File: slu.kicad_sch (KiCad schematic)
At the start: 166 parts, among them sw1 sw_2pos

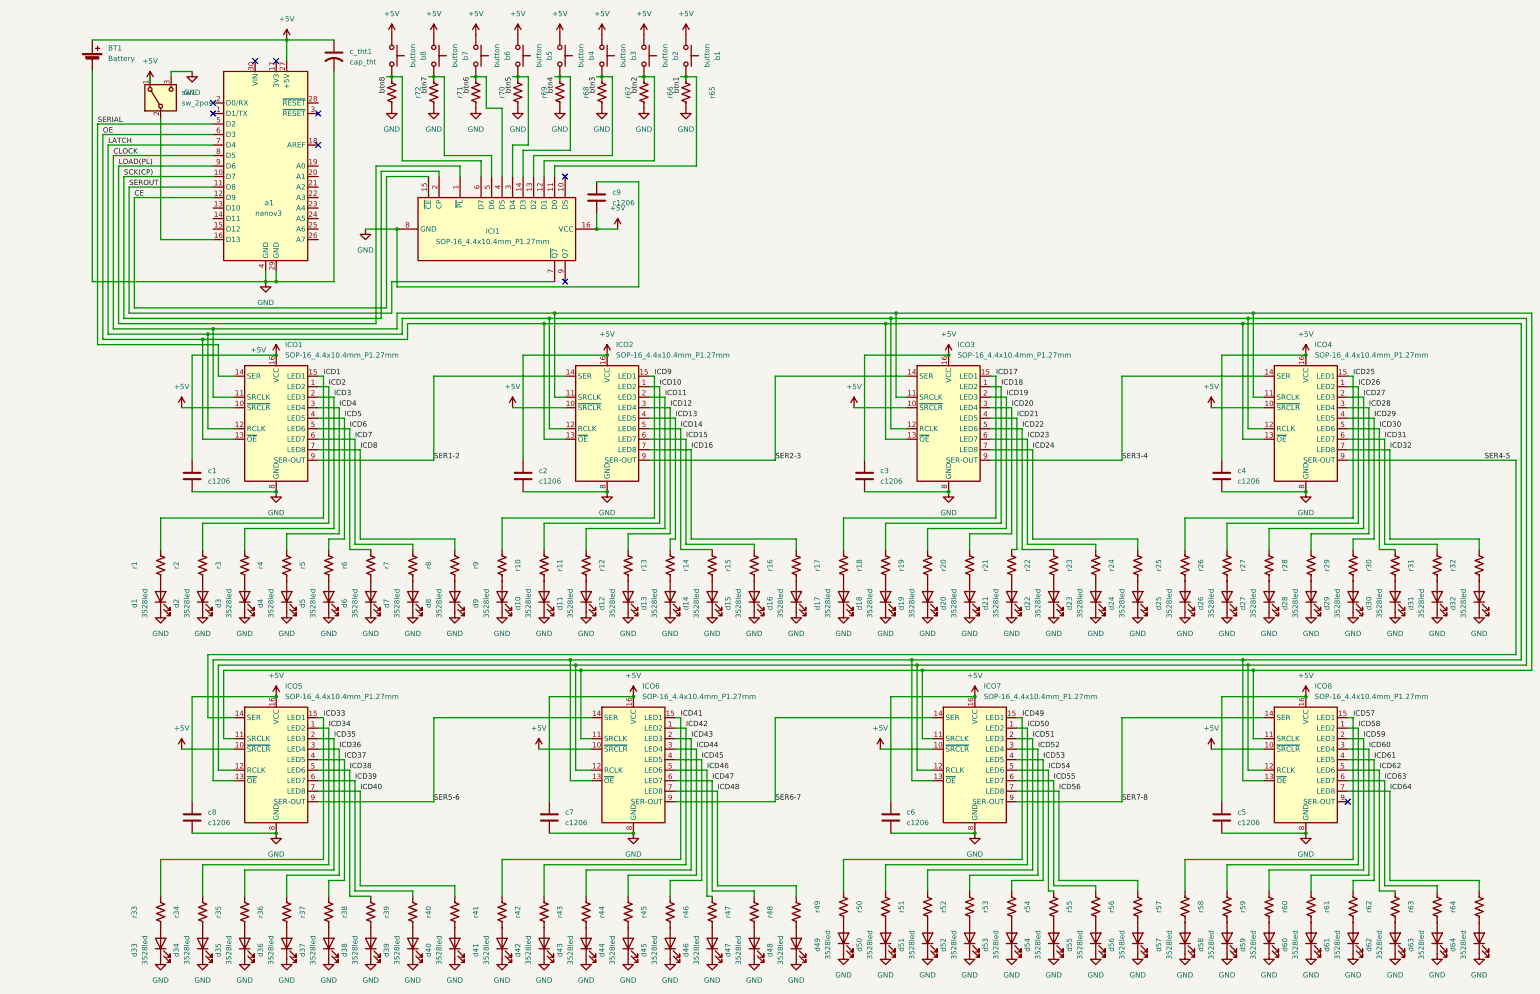
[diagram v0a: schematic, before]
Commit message: first finished draft all tracks connected
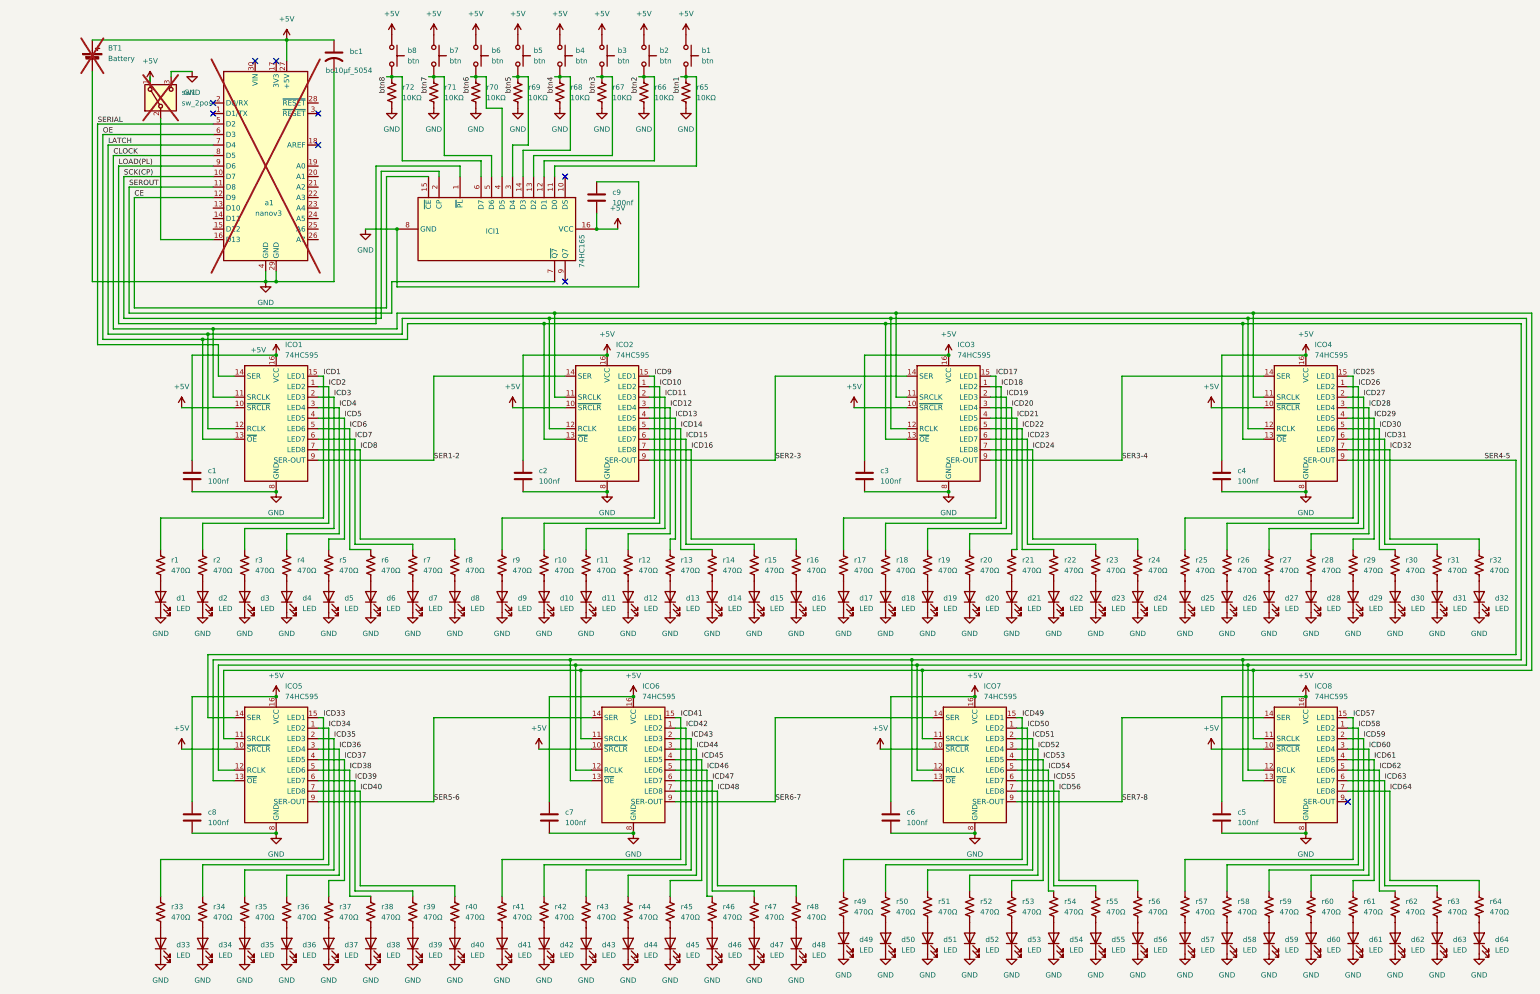
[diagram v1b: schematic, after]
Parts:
- BT1, a1, sw1: now not fitted; now left out of the parts list
- ICI1: value SOP-16_4.4x10.4mm_P1.27mm -> 74HC165; footprint Package_SO:SO-16_3.9x9.9mm_P1.27mm -> slu_leds_lib:sop16_hc165; symbol a_detolib_sym:74HC165 -> slu_leds_sym:ici_hc165; JLCPCB Part# (none) -> C22384789
- ICO1, ICO2, ICO3, ICO4, ICO5, ICO6, ICO7, ICO8: value SOP-16_4.4x10.4mm_P1.27mm -> 74HC595; footprint Package_SO:SOP-16_4.4x10.4mm_P1.27mm -> slu_leds_lib:sop16_hc595; symbol a_detolib_sym:74HC595D -> slu_leds_sym:ico_hc595; JLCPCB Part# (none) -> C10092
- b1, b2, b3, b4, b5, b6, b7, b8: value button -> btn; footprint a_detolib:btn_4x3 -> slu_leds_lib:btn_4x3; symbol a_detolib_sym:button -> slu_leds_sym:btn; JLCPCB Part# (none) -> C720477
- bc1: renamed from c_tht1; value cap_tht -> bc10µf_5054; footprint a_detolib:CP_Elec_5x5.4 -> slu_leds_lib:bulkcap_smd; symbol a_detolib_sym:bulk_cap_smd -> slu_leds_sym:bc10µf_5054; JLCPCB Part# (none) -> C72487
- c1, c2, c3, c4, c5, c6, c7, c8, c9: value c1206 -> 100nf; symbol a_detolib_sym:c1206 -> slu_leds_sym:c100nf_1206; JLCPCB Part# (none) -> C24497
- d1, d10, d11, d12, d13, d14, d15, d16, d17, d18, d19, d2, d20, d21, d22, d23, d24, d25, d26, d27, d28, d29, d3, d30, d31, d32, d33, d34, d35, d36, d37, d38, d39, d4, d40, d41, d42, d43, d44, d45, d46, d47, d48, d49, d5, d50, d51, d52, d53, d54, d55, d56, d57, d58, d59, d6, d60, d61, d62, d63, d64, d7, d8, d9: value 3528led -> LED; footprint a_detolib:3528led -> slu_leds_lib:blue_led_3528; symbol a_detolib_sym:led_3528 -> slu_leds_sym:led_3528; JLCPCB Part# (none) -> C2843802
- r1, r10, r11, r12, r13, r14, r15, r16, r17, r18, r19, r2, r20, r21, r22, r23, r24, r25, r26, r27, r28, r29, r3, r30, r31, r32, r33, r34, r35, r36, r37, r38, r39, r4, r40, r41, r42, r43, r44, r45, r46, r47, r48, r49, r5, r50, r51, r52, r53, r54, r55, r56, r57, r58, r59, r6, r60, r61, r62, r63, r64, r7, r8, r9: value ~ -> 470Ω; footprint a_detolib:r1206 -> slu_leds_lib:r_470Ω_1206; symbol a_detolib_sym:r1206 -> slu_leds_sym:r470_1206; JLCPCB Part# (none) -> C4502
- r65, r66, r67, r68, r69, r70, r71, r72: value ~ -> 10KΩ; footprint a_detolib:r1206 -> slu_leds_lib:r_10KΩ_1206; symbol a_detolib_sym:r1206 -> slu_leds_sym:r10k_1206; JLCPCB Part# (none) -> C17902

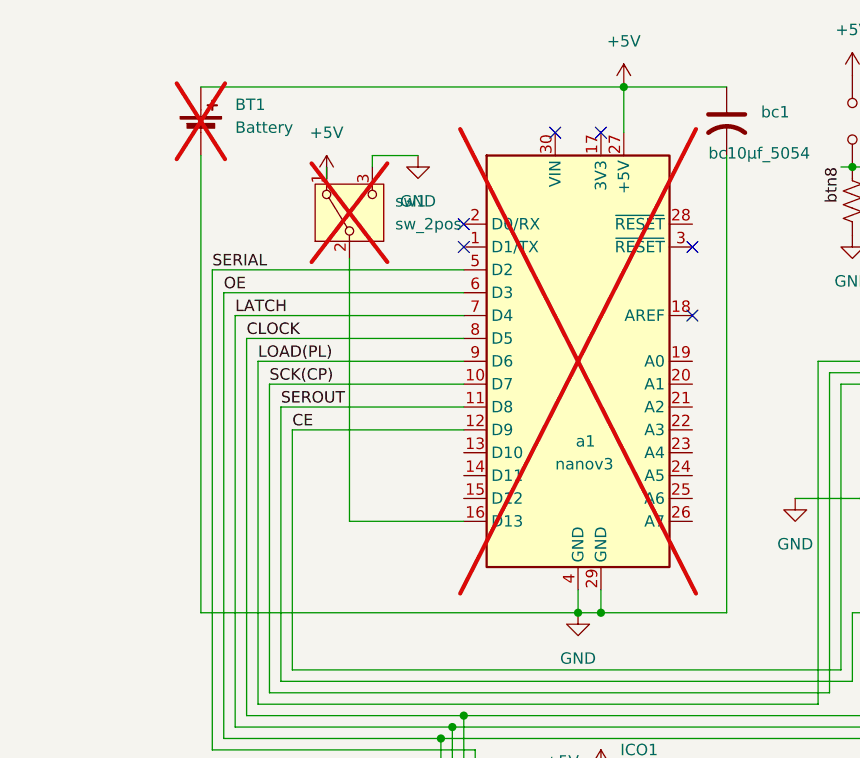
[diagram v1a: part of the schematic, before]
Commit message: most drc flags fixed
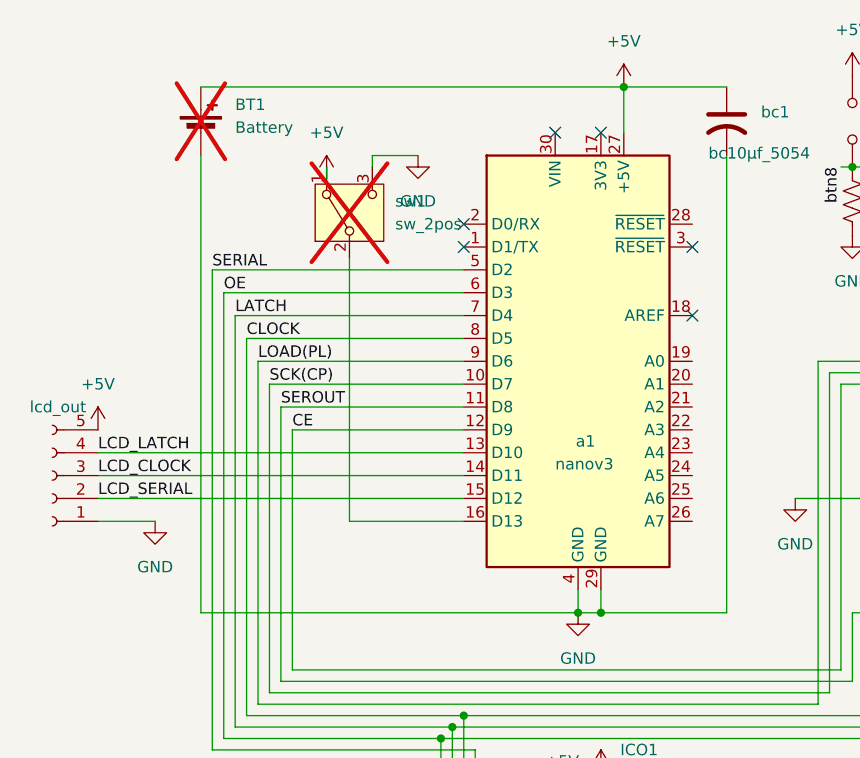
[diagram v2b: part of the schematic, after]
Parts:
- added J1: lcd_out, a_detolib:5pin_2.54, symbol slu_leds_sym:lcd_out
- a1: now fitted
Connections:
- net +5V: now also J1.5 (Pin_5)
- net GND: now also J1.1 (Pin_1)
- net LCD_LATCH: now reaches a1.13 (D10)
- net LCD_LATCH: now also J1.4 (Pin_4)
- net LCD_CLOCK: now reaches a1.14 (D11)
- net LCD_CLOCK: now also J1.3 (Pin_3)
- net LCD_SERIAL: now reaches a1.15 (D12)
- net LCD_SERIAL: now also J1.2 (Pin_2)

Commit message: almost done
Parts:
- added DIO1: SS34, slu_leds_lib:D_SMA, symbol slu_leds_sym:SS34
- BT1: footprint a_detolib:btry_18650_foirot -> slu_leds_lib:btry_18650_foirot; now fitted
- sw1: now fitted
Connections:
- net +5V: now also DIO1.1 (K); no longer BT1.1 (+)
- new net battery power: BT1.1 (+), DIO1.2 (A)
- no-connect marks 9 -> 18
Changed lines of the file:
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@@
 	)
 	(no_connect
+		(at 86.36 60.96)
+	)
+	(no_connect
 		(at 60.96 40.64)
 	)
@@
 	)
 	(no_connect
+		(at 86.36 68.58)
+	)
+	(no_connect
+		(at 86.36 63.5)
+	)
+	(no_connect
 		(at 60.96 38.1)
 	)
@@
 	)
 	(no_connect
+		(at 86.36 71.12)
+	)
+	(no_connect
+		(at 86.36 53.34)
+	)
+	(no_connect
+		(at 86.36 66.04)
+	)
+	(no_connect
+		(at 86.36 55.88)
+	)
+	(no_connect
+		(at 86.36 38.1)
+	)
+	(no_connect
 		(at 86.36 48.26)
 	)
@@
 		(at 146.05 55.88)
 	)
+	(no_connect
+		(at 86.36 58.42)
+	)
 	(wire
 		(pts
@@
 	(wire
 		(pts
-			(xy 31.75 22.86) (xy 78.74 22.86)
+			(xy 90.17 223.52) (xy 68.58 223.52)
 		)
 		(stroke
@@
 	(wire
 		(pts
-			(xy 90.17 223.52) (xy 68.58 223.52)
+			(xy 53.34 22.86) (xy 78.74 22.86)
 		)
 		(stroke
@@
 	(wire
 		(pts
-			(xy 31.75 30.48) (xy 31.75 81.28)
+			(xy 31.75 34.29) (xy 31.75 81.28)
 		)
 		(stroke
@@
 	(wire
 		(pts
+			(xy 31.75 22.86) (xy 45.72 22.86)
+		)
+		(stroke
+			(width 0)
+			(type default)
+		)
+	)
+	(wire
+		(pts
 			(xy 226.06 88.9) (xy 226.06 109.22)
 		)
@@
 	(wire
 		(pts
+			(xy 31.75 26.67) (xy 31.75 22.86)
+		)
+		(stroke
+			(width 0)
+			(type default)
+		)
+	)
+	(wire
+		(pts
 			(xy 176.53 223.52) (xy 151.13 223.52)
 		)
@@
 		)
 	)
+	(label "battery power"
+		(at 31.75 22.86 0)
+		(effects
+			(font
+				(size 1.27 1.27)
+			)
+			(justify left bottom)
+		)
+	)
 	(label "ICD11"
 		(at 170.18 109.22 0)
@@
 	(symbol
 		(lib_id "a_detolib_sym:battery_cell")
-		(at 31.75 27.94 0)
+		(at 31.75 31.75 0)
 		(unit 1)
 		(exclude_from_sim no)
 		(in_bom no)
 		(on_board yes)
-		(dnp yes)
-		(fields_autoplaced yes)
+		(dnp no)
 		(property "Reference" "BT1"
-			(at 35.56 24.8284 0)
+			(at 35.306 29.21 0)
 			(effects
 				(font
@@
 		)
 		(property "Value" "Battery"
-			(at 35.56 27.3684 0)
+			(at 35.56 31.1784 0)
 			(effects
 				(font
@@
 			)
 		)
-		(property "Footprint" "a_detolib:btry_18650_foirot"
-			(at 31.75 26.416 90)
+		(property "Footprint" "slu_leds_lib:btry_18650_foirot"
+			(at 31.75 30.226 90)
 			(effects
 				(font
@@
 		)
 		(property "Datasheet" "~"
-			(at 31.75 26.416 90)
+			(at 31.75 30.226 90)
 			(effects
 				(font
@@
 		)
 		(property "Description" "Single-cell battery"
-			(at 31.75 27.94 0)
+			(at 31.75 31.75 0)
 			(effects
 				(font
@@
 		(in_bom no)
 		(on_board yes)
-		(dnp yes)
+		(dnp no)
 		(fields_autoplaced yes)
 		(property "Reference" "sw1"
@@
 					(unit 1)
 				)
+			)
+		)
+	)
+	(symbol
+		(lib_id "slu_leds_sym:SS34")
+		(at 49.53 22.86 180)
+		(unit 1)
+		(exclude_from_sim no)
+		(in_bom yes)
+		(on_board yes)
+		(dnp no)
+		(property "Reference" "DIO1"
+			(at 49.784 17.78 0)
+			(effects
+				(font
+					(size 1.27 1.27)
+				)
+			)
+		)
+		(property "Value" "SS34"
+			(at 49.784 20.32 0)
+			(effects
+				(font
+					(size 1.27 1.27)
+				)
+			)
+		)
+		(property "Footprint" "slu_leds_lib:D_SMA"
+			(at 49.8475 19.05 0)
+			(effects
+				(font
+					(size 1.27 1.27)
+				)
+				(hide yes)
+			)
+		)
+		(property "Datasheet" "https://www.vishay.com/docs/88751/ss32.pdf"
+			(at 49.53 22.86 0)
+			(effects
+				(font
+					(size 1.27 1.27)
+				)
+				(hide yes)
+			)
+		)
+		(property "Description" "40V 3A Schottky Diode, SMA"
+			(at 49.53 22.86 0)
+			(effects
+				(font
+					(size 1.27 1.27)
+				)
+				(hide yes)
+			)
+		)
+		(pin "2"
+		)
+		(pin "1"
+		)
+		(instances
+			(project ""
+				(path "/783ad4de-863e-46d6-9f57-d8e7f09a6eb3"
+					(reference "DIO1")
+					(unit 1)
+				)

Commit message: added mount holes for battery
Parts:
- bc1: footprint slu_leds_lib:bulkcap_smd -> slu_leds_lib:CP_Elec_4x5.4
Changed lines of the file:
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@@
 			)
 		)
-		(property "Footprint" "slu_leds_lib:bulkcap_smd"
+		(property "Footprint" "slu_leds_lib:CP_Elec_4x5.4"
 			(at 90.17 26.67 0)
 			(effects

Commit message: recovery after jlc order
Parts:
- BT1, a1, sw1: now not fitted
- DIO1: LCSC Part # (none) -> C8678
- ICI1: JLCPCB Part# C22384789 -> (none); LCSC Part # (none) -> C61060
- ICO1, ICO2, ICO3, ICO4, ICO5, ICO6, ICO7, ICO8: JLCPCB Part# C10092 -> (none); LCSC Part # (none) -> C79097
- J1: now not fitted; now left out of the parts list
- b1, b2, b3, b4, b5, b6, b7, b8: JLCPCB Part# C720477 -> (none); LCSC Part # (none) -> C720477
- bc1: JLCPCB Part# C72487 -> (none); LCSC Part # (none) -> C3343
- c1, c2, c3, c4, c5, c6, c7, c8, c9: JLCPCB Part# C24497 -> (none); LCSC Part # (none) -> C24497
- d1, d10, d11, d12, d13, d14, d15, d16, d17, d18, d19, d2, d20, d21, d22, d23, d24, d25, d26, d27, d28, d29, d3, d30, d31, d32, d33, d34, d35, d36, d37, d38, d39, d4, d40, d41, d42, d43, d44, d45, d46, d47, d48, d49, d5, d50, d51, d52, d53, d54, d55, d56, d57, d58, d59, d6, d60, d61, d62, d63, d64, d7, d8, d9: JLCPCB Part# C2843802 -> (none); LCSC Part # (none) -> C50327302
- r1, r10, r11, r12, r13, r14, r15, r16, r17, r18, r19, r2, r20, r21, r22, r23, r24, r25, r26, r27, r28, r29, r3, r30, r31, r32, r33, r34, r35, r36, r37, r38, r39, r4, r40, r41, r42, r43, r44, r45, r46, r47, r48, r49, r5, r50, r51, r52, r53, r54, r55, r56, r57, r58, r59, r6, r60, r61, r62, r63, r64, r7, r8, r9: JLCPCB Part# C4502 -> (none); LCSC Part # (none) -> C4502
- r65, r66, r67, r68, r69, r70, r71, r72: JLCPCB Part# C17902 -> (none); LCSC Part # (none) -> C17902
